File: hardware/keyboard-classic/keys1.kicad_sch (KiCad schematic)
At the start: 58 parts, among them SW33 Break, SW35 R_Shift, SW36 P, SW37 Comma, SW38 K, SW39 L_Shift, SW40 Semicolon, SW41 M, SW42 J, SW43 Fwd_Slash, SW44 N, SW45 H, SW46 SPACE, SW47 B, SW48 G, SW49 TAB, SW50 Z, SW51 V, SW52 F, SW53 CTRL, SW54 A, SW55 C, SW56 D, SW57 Backslash, SW58 Q, SW59 X, SW60 S, SW62 ESC, SW63 Spare

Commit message: Add some mounting hardware
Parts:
- D1, D34, D35, D36, D37, D38, D39, D40, D41, D42, D43, D44, D45, D46, D47, D48, D49, D50, D51, D52, D53, D54, D55, D56, D57, D58, D59, D60, D61: Manufacturer PN (none) -> MMBD914LT3G
- SW33, SW62, SW63: symbol Switch:SW_Push -> unikbd:SW Cherry MX/Futaba 1U Style A; Allow Substitution (none) -> Yes; Class (none) -> If applicable; Component Type (none) -> Switch; Component Value (none) -> Key; Fitted NO -> Yes; Manufacturer (none) -> Cherry; Manufacturer Link (none) -> https://www.cherrymx.de/en/cherry-mx/mx-original/mx-black.h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; Manufacturer PN (none) -> MX1A-11NN; Material (none) -> If applicable; Number of Pins (none) -> 2; Power Rating (none) -> 10 mA; RoHS (none) -> Yes; RoHS Document Link (none) -> https://www.mouser.com/catalog/additional/Cherry_Electrical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; Standards Version (none) -> 1.1; Temp (Operating) (none) -> -40C/+170C; Temp (Soldering) (none) -> If applicable; Temp Coeff. (none) -> If applicable; Tolerance (none) -> If applicable; Tracking (none) -> No
- SW35, SW39: symbol Switch:SW_Push -> unikbd:SW Cherry MX/Futaba 1U Style A; Allow Substitution (none) -> Yes; BOM Comment (none) -> 1.5U; Class (none) -> If applicable; Component Type (none) -> Switch; Component Value (none) -> Key; Manufacturer (none) -> Cherry; Manufacturer Link (none) -> https://www.cherrymx.de/en/cherry-mx/mx-original/mx-black.h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; Manufacturer PN (none) -> MX1A-11NN; Material (none) -> If applicable; Number of Pins (none) -> 2; Power Rating (none) -> 10 mA; RoHS (none) -> Yes; RoHS Document Link (none) -> https://www.mouser.com/catalog/additional/Cherry_Electrical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; Standards Version (none) -> 1.1; Temp (Operating) (none) -> -40C/+170C; Temp (Soldering) (none) -> If applicable; Temp Coeff. (none) -> If applicable; Tolerance (none) -> If applicable; Tracking (none) -> No
- SW36, SW37, SW38, SW40, SW41, SW42, SW43, SW44, SW45, SW47, SW48, SW49, SW50, SW51, SW52, SW53, SW54, SW55, SW56, SW57, SW58, SW59, SW60: symbol Switch:SW_Push -> unikbd:SW Cherry MX/Futaba 1U Style A; Allow Substitution (none) -> Yes; Class (none) -> If applicable; Component Type (none) -> Switch; Component Value (none) -> Key; Manufacturer (none) -> Cherry; Manufacturer Link (none) -> https://www.cherrymx.de/en/cherry-mx/mx-original/mx-black.h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; Manufacturer PN (none) -> MX1A-11NN; Material (none) -> If applicable; Number of Pins (none) -> 2; Power Rating (none) -> 10 mA; RoHS (none) -> Yes; RoHS Document Link (none) -> https://www.mouser.com/catalog/additional/Cherry_Electrical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; Standards Version (none) -> 1.1; Temp (Operating) (none) -> -40C/+170C; Temp (Soldering) (none) -> If applicable; Temp Coeff. (none) -> If applicable; Tolerance (none) -> If applicable; Tracking (none) -> No
- SW46: symbol Switch:SW_Push -> unikbd:SW Cherry MX/Futaba 8U Spacebar Style A; Allow Substitution (none) -> Yes; BOM Comment (none) -> 8U spacebar; Class (none) -> If applicable; Component Type (none) -> Switch; Component Value (none) -> Key; Manufacturer (none) -> Cherry; Manufacturer Link (none) -> https://www.cherrymx.de/en/cherry-mx/mx-original/mx-black.h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; Manufacturer PN (none) -> MX1A-11NN; Material (none) -> If applicable; Number of Pins (none) -> 2; Power Rating (none) -> 10 mA; RoHS (none) -> Yes; RoHS Document Link (none) -> https://www.mouser.com/catalog/additional/Cherry_Electrical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; Standards Version (none) -> 1.1; Temp (Operating) (none) -> -40C/+170C; Temp (Soldering) (none) -> If applicable; Temp Coeff. (none) -> If applicable; Tolerance (none) -> If applicable; Tracking (none) -> No

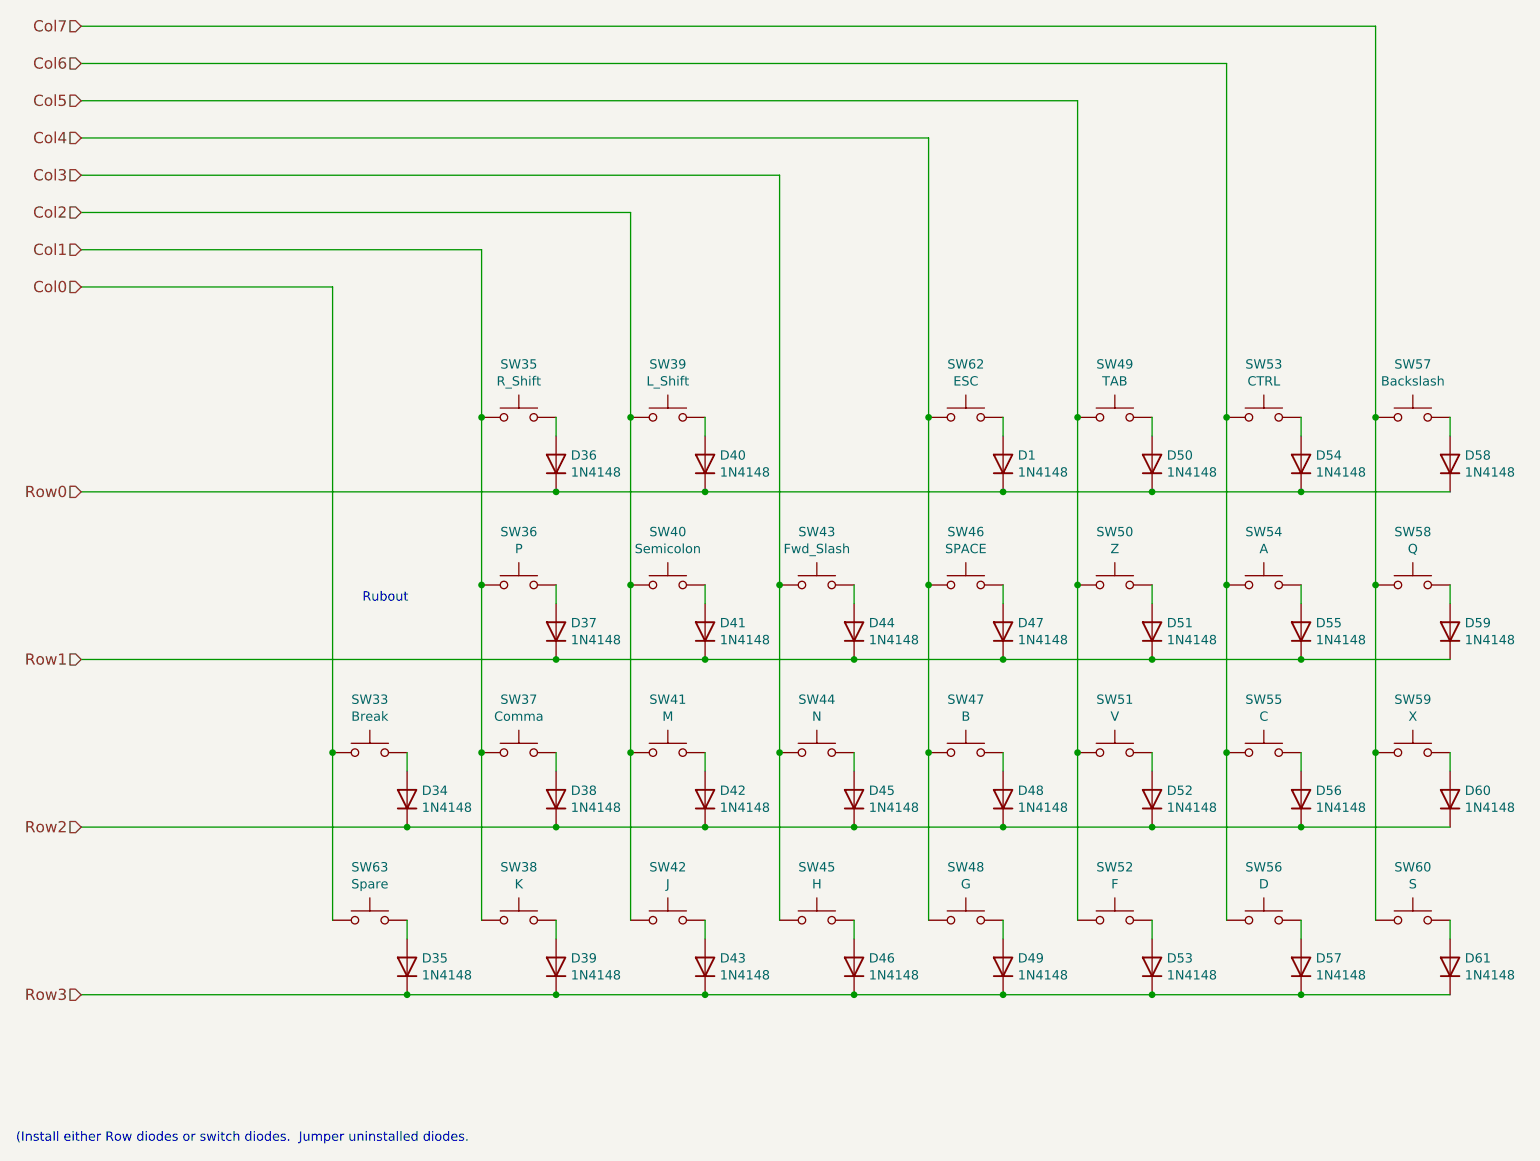
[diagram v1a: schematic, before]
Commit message: Update to include mounting hardware
- Fix all components to include full information including BOM
information

- Include all mounting hardware in components List

- fix schematic to align on 0.1" grid.
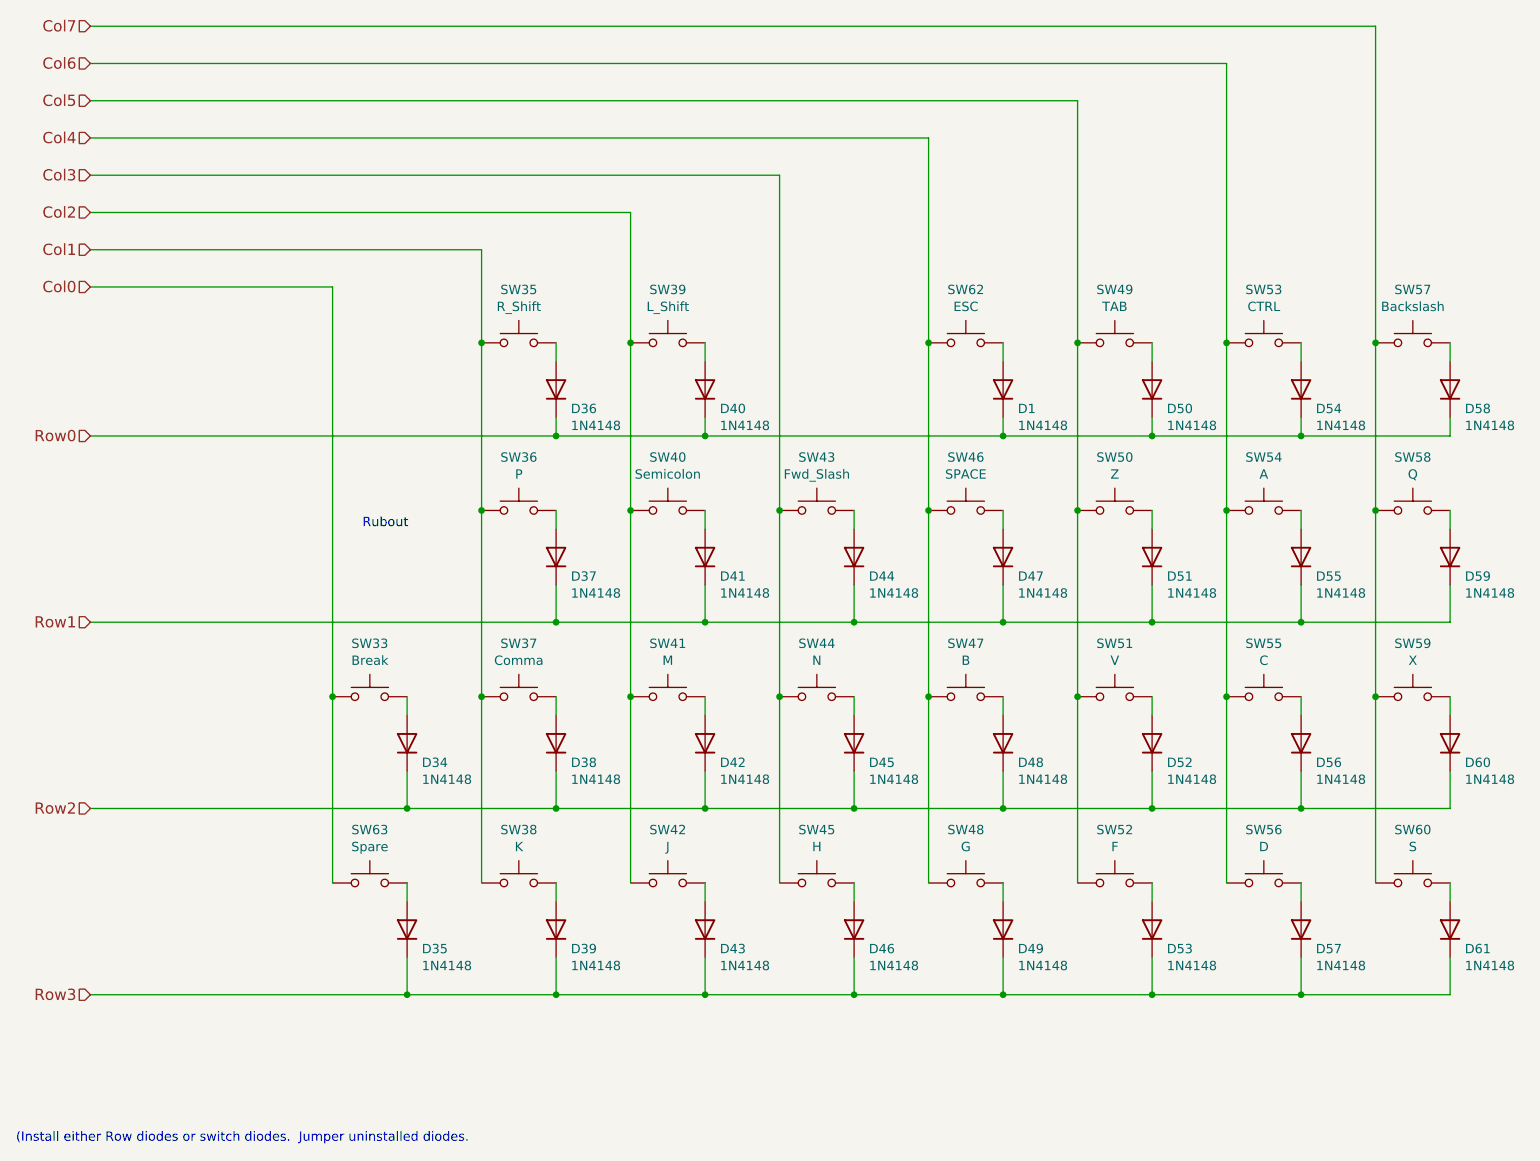
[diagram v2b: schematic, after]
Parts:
- D1, D34, D35, D36, D37, D38, D39, D40, D41, D42, D43, D44, D45, D46, D47, D48, D49, D50, D51, D52, D53, D54, D55, D56, D57, D58, D59, D60, D61: Allow Substitution (none) -> Yes; BOM Comment (none) -> Either SMT or Through-Hole part (1n914 or 1n4148) is fitted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; Class (none) -> If applicable; Component Type (none) -> Diode; Component Value (none) -> 19N14/MMBD914; Fitted YES -> Yes; Manufacturer ON Semiconductor -> Diodes, Inc.; Manufacturer Link (none) -> https://www.diodes.com/part/view/MMBD914; Manufacturer PN MMBD914LT3G -> MMBD914-7-F; Material (none) -> If applicable; Number of Pins (none) -> 3; Package Type (none) -> SOT3-3; Power Rating (none) -> 350 mW / 200 mA; RoHS (none) -> Yes; RoHS Document Link (none) -> https://www.diodes.com/assets/Quality-Reliability-Docs/Mast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; Standards Version (none) -> 1.1; Temp (Operating) (none) -> -65C/150C; Temp (Soldering) (none) -> If applicable; Temp (Storage) (none) -> If applicable; Temp Coeff. (none) -> If applicable; Tolerance (none) -> If applicable; Tracking (none) -> No
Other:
- moved on the sheet: D1, D34, D35, D36, D37, D38, D39, D40, D41, D42, D43, D44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
